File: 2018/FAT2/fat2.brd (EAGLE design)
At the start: 160 x 100 mm, 30 parts, among them Q1 BUZ11BV, Q2 BUZ11BV, U1 TSR_1-2450, U2 TSR_1-2450, U3 TSR_1-2433

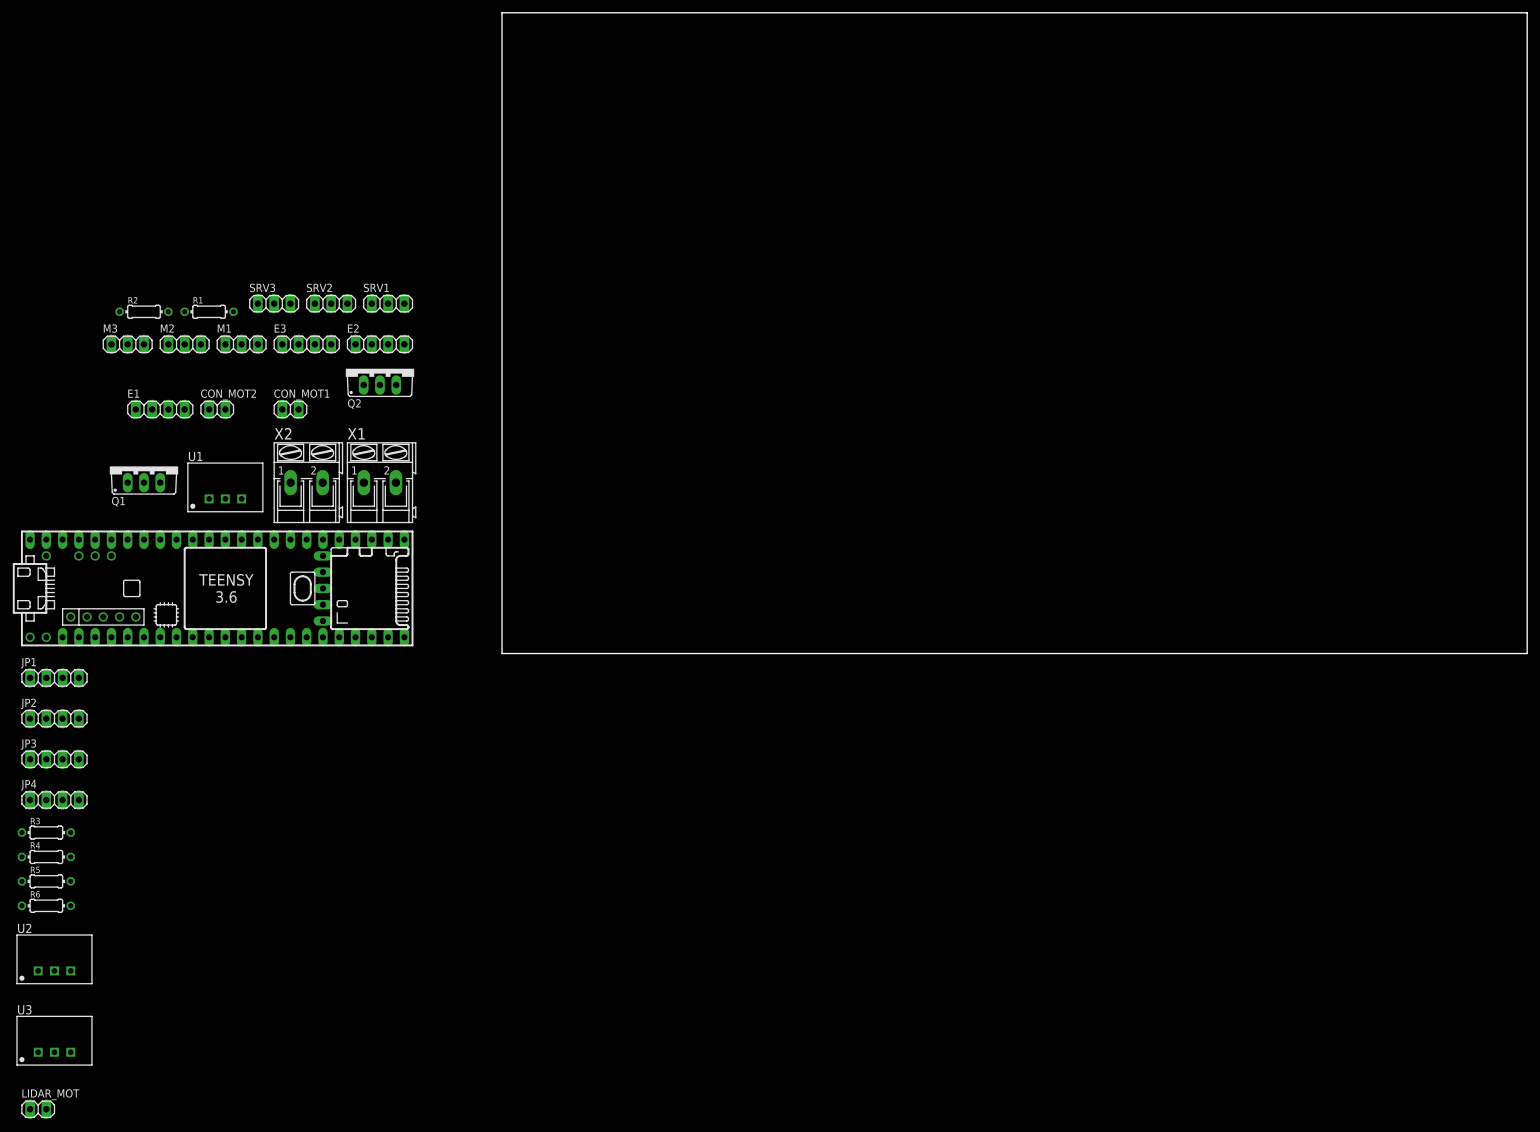
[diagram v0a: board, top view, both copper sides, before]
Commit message: [FAT V2] Route easy side.
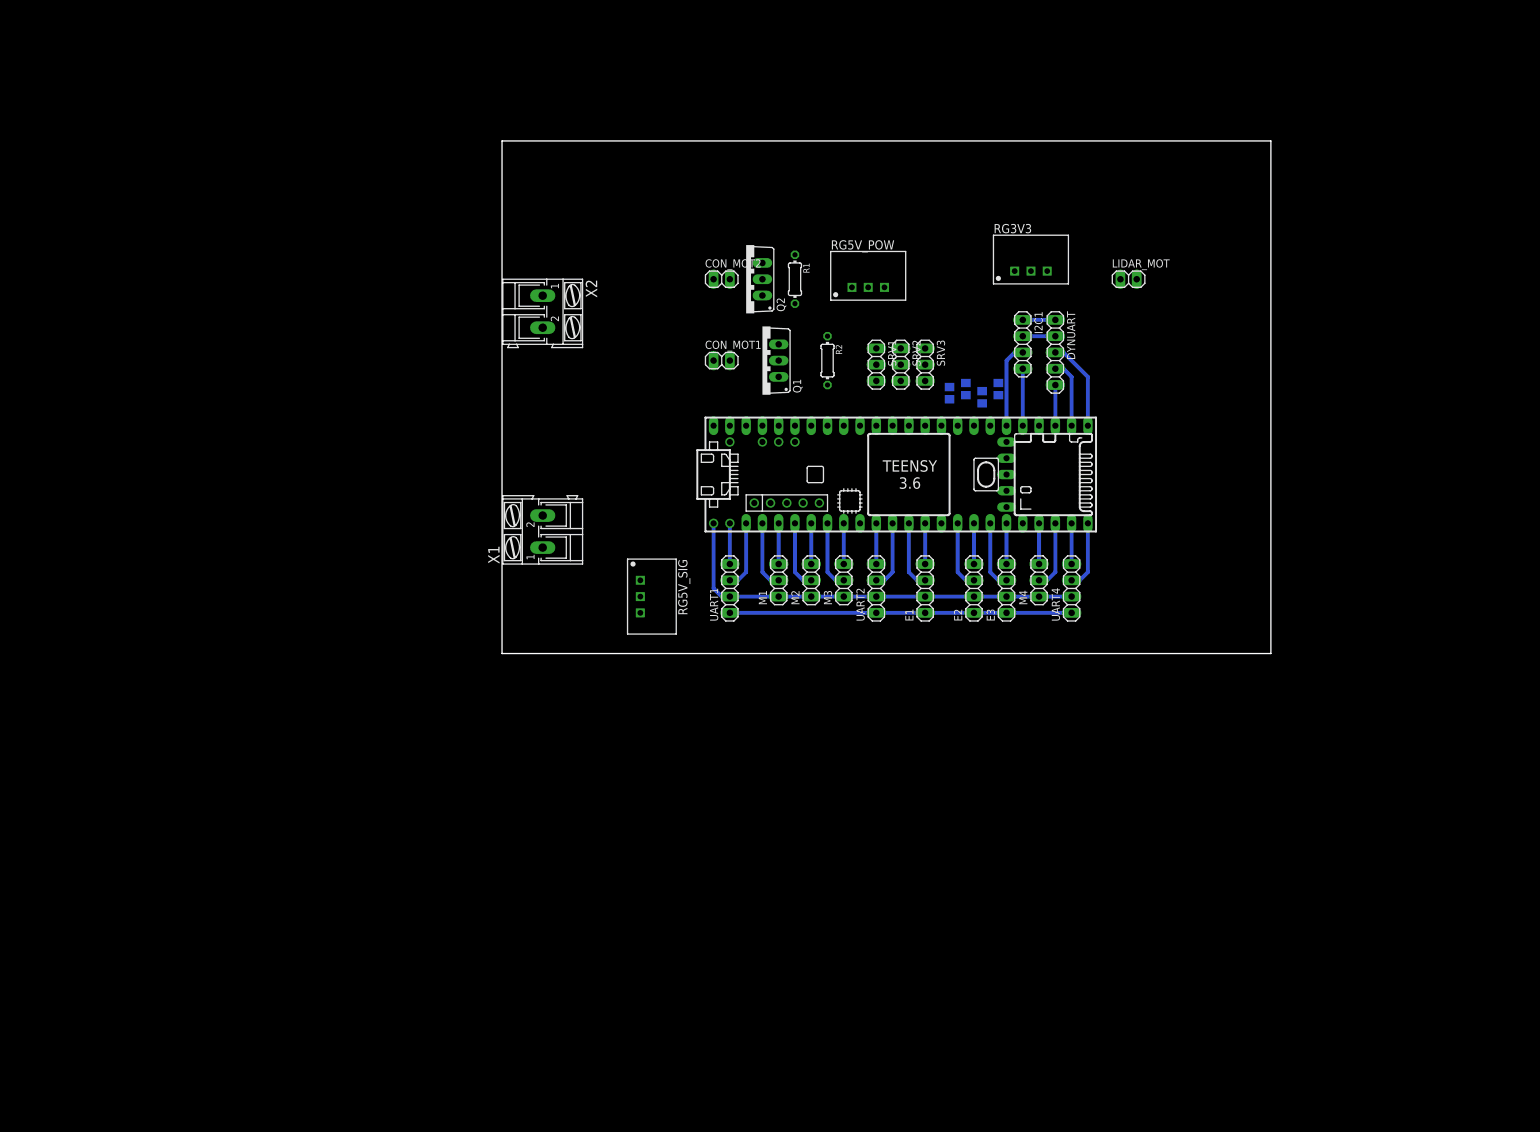
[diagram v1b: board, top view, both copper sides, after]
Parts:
- removed JP1, JP2, JP3, JP4: (no value), pinhead:1X04
- removed U1, U2: TSR_1-2450, _traco_tsr-1:TSR-1
- removed U3: TSR_1-2433, _traco_tsr-1:TSR-1
- added DYNUART: (no value), pinhead:1X05
- added I2C1, UART1, UART2, UART4: (no value), pinhead:1X04
- added M4: (no value), pinhead:1X03
- added RG3V3: TSR_1-2433, _traco_tsr-1:TSR-1
- added RG5V_POW, RG5V_SIG: TSR_1-2450, _traco_tsr-1:TSR-1
- R3, R4, R5, R6: value 10k -> (none); device rcl:0204/7 -> rcl:R0805
- moved LIDAR_MOT 213.9 mm to (97.8, 58.4)
- moved R5 167.3 mm to (77.5, 41.3), flipped to the bottom, turned to 90 degrees
- moved R6 166.2 mm to (74.9, 40.0), flipped to the bottom, turned to 270 degrees
- moved R4 161.0 mm to (72.4, 41.3), flipped to the bottom, turned to 90 degrees
- moved R3 156.8 mm to (69.8, 40.6), flipped to the bottom, turned to 270 degrees
- moved E1 122.6 mm to (66.0, 10.2), turned to 90 degrees
- moved M3 117.7 mm to (53.3, 11.4), turned to 90 degrees
- moved E3 115.7 mm to (78.7, 10.2), turned to 90 degrees
- moved U$1 108.2 mm to (61.0, 27.9)
- moved R2 107.0 mm to (50.8, 45.7), turned to 270 degrees
- moved M2 104.5 mm to (48.3, 11.4), turned to 90 degrees
- moved SRV3 102.0 mm to (66.0, 45.1), turned to 270 degrees
- moved E2 100.2 mm to (73.7, 10.2), turned to 90 degrees
- moved Q1 97.9 mm to (40.6, 45.7), turned to 90 degrees
- moved R1 91.6 mm to (45.7, 58.4), turned to 270 degrees
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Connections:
- removed net N$10: JP2.1
- removed net N$11: JP2.2
- removed net N$12: JP2.3
- removed net N$13: JP2.4
- new net 29: M4.3, U$1.29
- new net 30: M4.2, U$1.30
- new net DYN_CTRL: DYNUART.5, U$1.35/A16
- new net N$6: U$1.17/A3
- new net RX2: U$1.9/CS, UART2.4
- new net RX4: U$1.31/A12, UART4.4
- new net RX5: DYNUART.4, U$1.34/A15
- new net SCL1: I2C1.4, U$1.37/A18
- new net SDA1: I2C1.3, U$1.38/A19
- new net TX2: U$1.10/CS, UART2.3
- new net TX4: U$1.32/A13, UART4.3
- new net TX5: DYNUART.3, U$1.33/A14
- net 12V_POW: now also RG3V3.1, RG5V_POW.1; no longer U2.1, U3.1
- net 12V_SIG: now also RG5V_SIG.1; no longer U1.1
- net 3V3: now also RG3V3.3; no longer U3.3
- net 5V_POW: now also RG5V_POW.3; no longer U2.3
- net 5V_SIG: now also DYNUART.1, I2C1.1, RG5V_SIG.3, UART1.1, UART2.1, UART4.1; no longer JP1.1, U1.3
- net DIR1: now also U$1.3/CANTX
- net DIR2: now also U$1.5
- net DIR3: now also U$1.7
- net ENC_1_A: now also U$1.11/MOSI
- net ENC_1_B: now also U$1.12/MISO
- net ENC_2_A: now also U$1.24
- net ENC_2_B: now also U$1.25
- net ENC_3_A: now also U$1.26
- net ENC_3_B: now also U$1.27
- net GND: now also DYNUART.2, I2C1.2, M4.1, RG3V3.2, RG5V_POW.2, RG5V_SIG.2, UART1.2, UART2.2, UART4.2; no longer JP1.2, U1.2, U2.2, U3.2
- net MOT1: now also U$1.22/A8
- net MOT2: now also U$1.23/A9
- net POW_LEVEL: now also U$1.A22/DAC1
- net PWM1: now also U$1.2
- net PWM2: now also U$1.4/CANRX
- net PWM3: now also U$1.6
- net RX1: now also UART1.4; no longer JP1.4
- net SERVO1: now also U$1.16/A2
- net SERVO2: now also U$1.15/A1
- net SERVO3: now also U$1.14/A0
- net SIG_LEVEL: now also U$1.21/DAC0
- net TX1: now also UART1.3; no longer JP1.3
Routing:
- net GND: track 0.00 -> 71.6 mm
- net 5V_SIG: track 0.00 -> 59.7 mm
- net TX5: track 0.00 -> 14.3 mm
- net SDA1: track 0.00 -> 13.2 mm
- net ENC_1_A: track 0.00 -> 10.7 mm
- net 30: track 0.00 -> 10.7 mm
- net PWM3: track 0.00 -> 10.7 mm
- net RX5: track 0.00 -> 10.7 mm
- net PWM1: track 0.00 -> 10.7 mm
- net TX2: track 0.00 -> 10.7 mm
- net TX1: track 0.00 -> 10.7 mm
- net PWM2: track 0.00 -> 10.7 mm
- net TX4: track 0.00 -> 10.7 mm
- net ENC_3_A: track 0.00 -> 10.7 mm
- net ENC_2_A: track 0.00 -> 10.7 mm
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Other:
- board size 160 x 100 mm -> 120 x 80 mm

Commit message: [FAT V2] Finish board.
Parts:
- removed R3, R4, R5, R6: (no value), rcl:R0805
- added JP1: (no value), pinhead:1X02/90
- added R10, R7, R8, R9: 10k, rcl:0204/7
- added SPARE: (no value), pinhead:1X05
- moved R1 22.6 mm to (31.8, 40.6), turned to 0 degrees
- moved CON_MOT1 18.9 mm to (40.6, 63.5), turned to 270 degrees
- moved Q2 11.9 mm to (33.0, 47.6), turned to 180 degrees
- moved Q1 11.4 mm to (40.6, 57.1), turned to 0 degrees
- moved R2 8.98 mm to (41.9, 47.0), turned to 180 degrees
- moved X2 8.98 mm to (7.62, 44.5), turned to 90 degrees
- moved RG5V_POW 8.03 mm to (49.5, 59.7), turned to 270 degrees
- moved LIDAR_MOT 7.73 mm to (90.2, 59.7), turned to 90 degrees
- moved X1 7.73 mm to (7.62, 11.4), turned to 270 degrees
- moved RG3V3 5.24 mm to (77.5, 61.0), turned to 270 degrees
- moved CON_MOT2 5.24 mm to (33.0, 63.5), turned to 270 degrees
- moved UART4 5.08 mm to (83.8, 10.2)
- moved E1 5.08 mm to (61.0, 10.2)
- moved M3 5.08 mm to (48.3, 11.4)
- moved UART1 5.08 mm to (30.5, 10.2)
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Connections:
- new net GND2: R10.1, R8.1, U$1.GND2
- new net N$1: SPARE.5, U$1.17/A3
- new net N$2: SPARE.4, U$1.18/A4/SDA
- new net N$4: SPARE.3, U$1.19/A5/SCL
- new net N$8: SPARE.1, U$1.21/A7
- net 12V_POW: now also R7.2; no longer R4.2
- net 12V_SIG: now also R9.2; no longer R5.2
- net 5V_SIG: now also JP1.1, U$1.VIN
- net GND: now also Q1.S, Q2.S, R1.1, R2.1; no longer R3.1, R6.1
- net N$6: now also SPARE.2, U$1.20/A6; no longer U$1.17/A3
- net N$7: now also JP1.2, U$1.VUSB; no longer Q1.S, Q2.S, R1.1, R2.1
- net POW_LEVEL: now also R7.1, R8.2; no longer R3.2, R4.1
- net SIG_LEVEL: now also R10.2, R9.1; no longer R5.1, R6.2
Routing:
- net GND: track 71.6 -> 276.5 mm, vias 0 -> 2
- net 12V_SIG: track 0.00 -> 161.0 mm, vias 0 -> 2
- net 5V_SIG: track 59.7 -> 164.5 mm, vias 0 -> 2
- net 12V_POW: track 0.00 -> 97.2 mm
- net 5V_POW: track 0.00 -> 22.0 mm
- net MOT1: track 0.00 -> 19.0 mm
- net POW_LEVEL: track 0.00 -> 15.5 mm
- net MOT2: track 0.00 -> 14.6 mm
- net SIG_LEVEL: track 0.00 -> 13.8 mm
- net 3V3: track 0.00 -> 12.7 mm
- net N$5: track 0.00 -> 12.1 mm
- net N$7: track 0.00 -> 9.20 mm
- net SERVO3: track 0.00 -> 8.94 mm
- net SERVO2: track 0.00 -> 8.41 mm
- net SERVO1: track 0.00 -> 7.88 mm
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- added copper zone on layer 16, net GND
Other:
- board size 120 x 80 mm -> 95.9 x 69.8 mm
- board text added: "FAT V2 - Fab@ENAC 18"
